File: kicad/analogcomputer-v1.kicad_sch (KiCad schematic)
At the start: 20 parts, among them U1 TL082, U2 TL082, U3 TL082, U4 TL082, U5 TL082

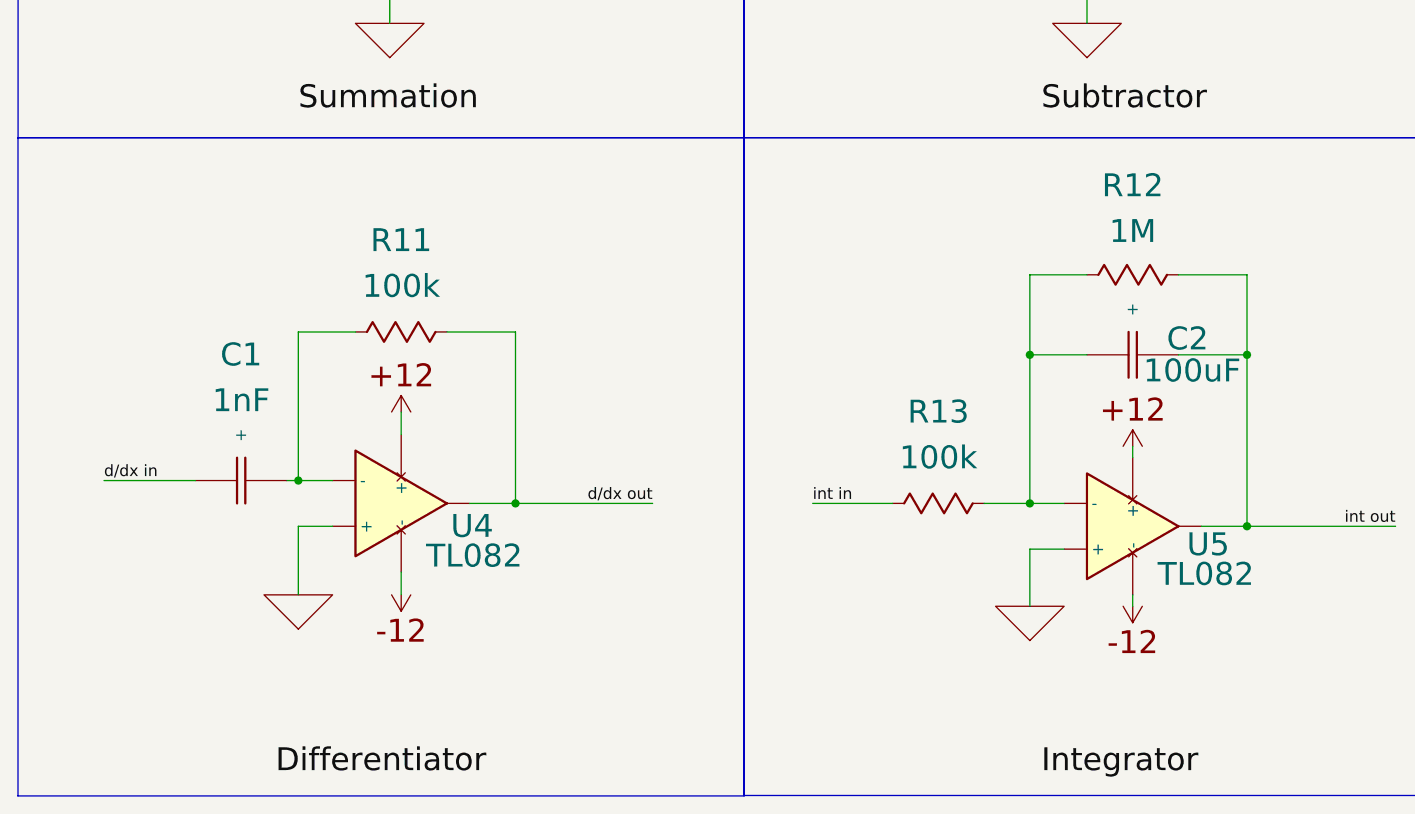
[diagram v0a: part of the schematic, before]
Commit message: updated differentiation circuit and spacing
Spacing of ins/outs, added input resistor to differentiation circuit.
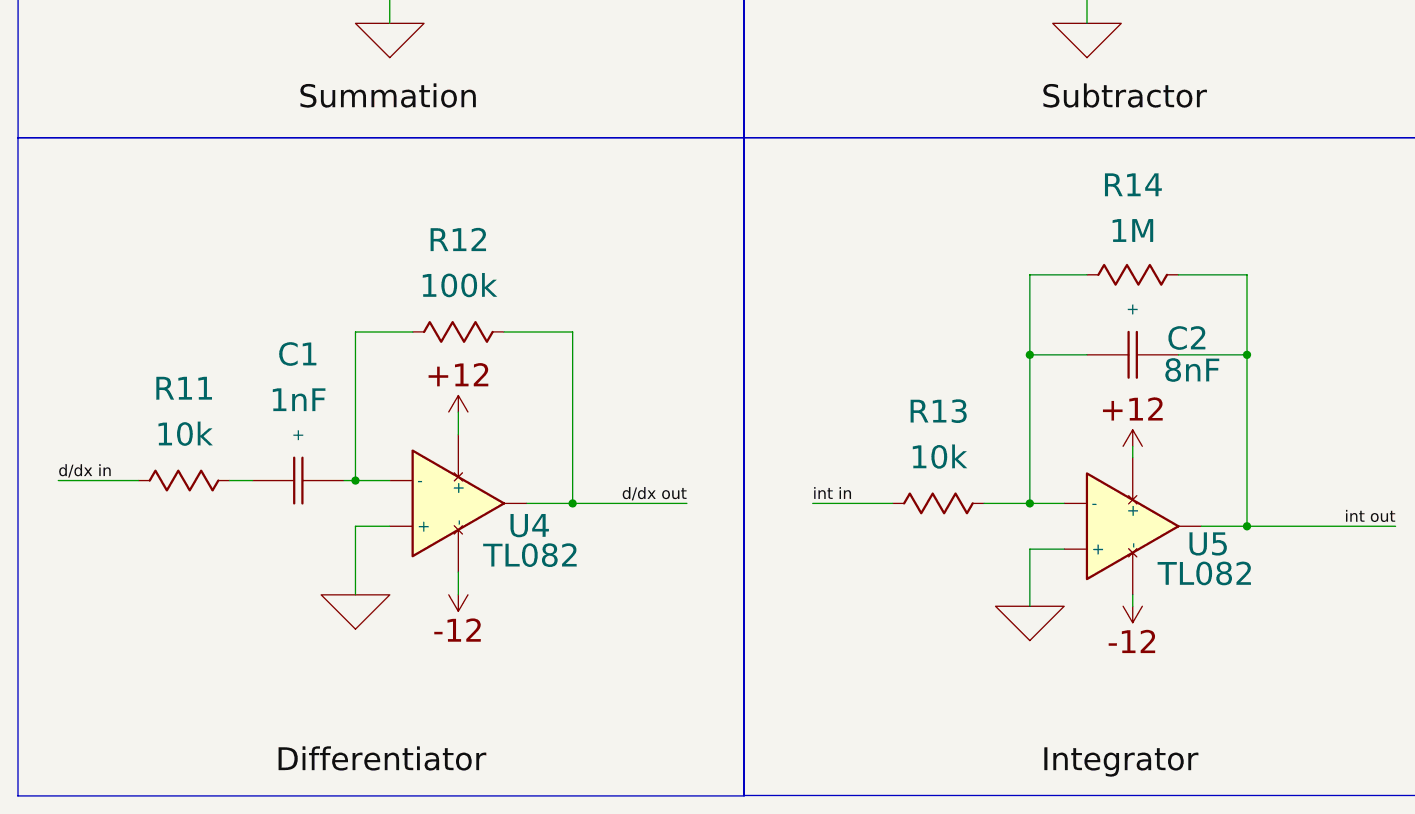
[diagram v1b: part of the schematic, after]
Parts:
- added R11: 10k, symbol PCM_Generic:R,IEEE
- C2: value 100uF -> 8nF
- R13: value 100k -> 10k
- renumbered R11 to R12, R12 to R14
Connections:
- net d/dx in: now also R11.1 (+); no longer C1.1 (+)
- new net: C1.1 (+), R11.2 (-)
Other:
- moved on the sheet: C1, R12, U4
